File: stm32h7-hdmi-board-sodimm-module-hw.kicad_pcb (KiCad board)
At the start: 6 copper layers, 67.6 x 27.8 mm, 90 parts, among them J1 PCB-Edge_SODIMM_144_SDR, U1 IS42S86400F-7TL, U10 24AA024_TDFN, U2 IS42S86400F-7TL, U3 IS42S86400F-7TL, U4 IS42S86400F-7TL, U5 IS42S86400F-7TL, U6 IS42S86400F-7TL, U7 IS42S86400F-7TL, U8 IS42S86400F-7TL

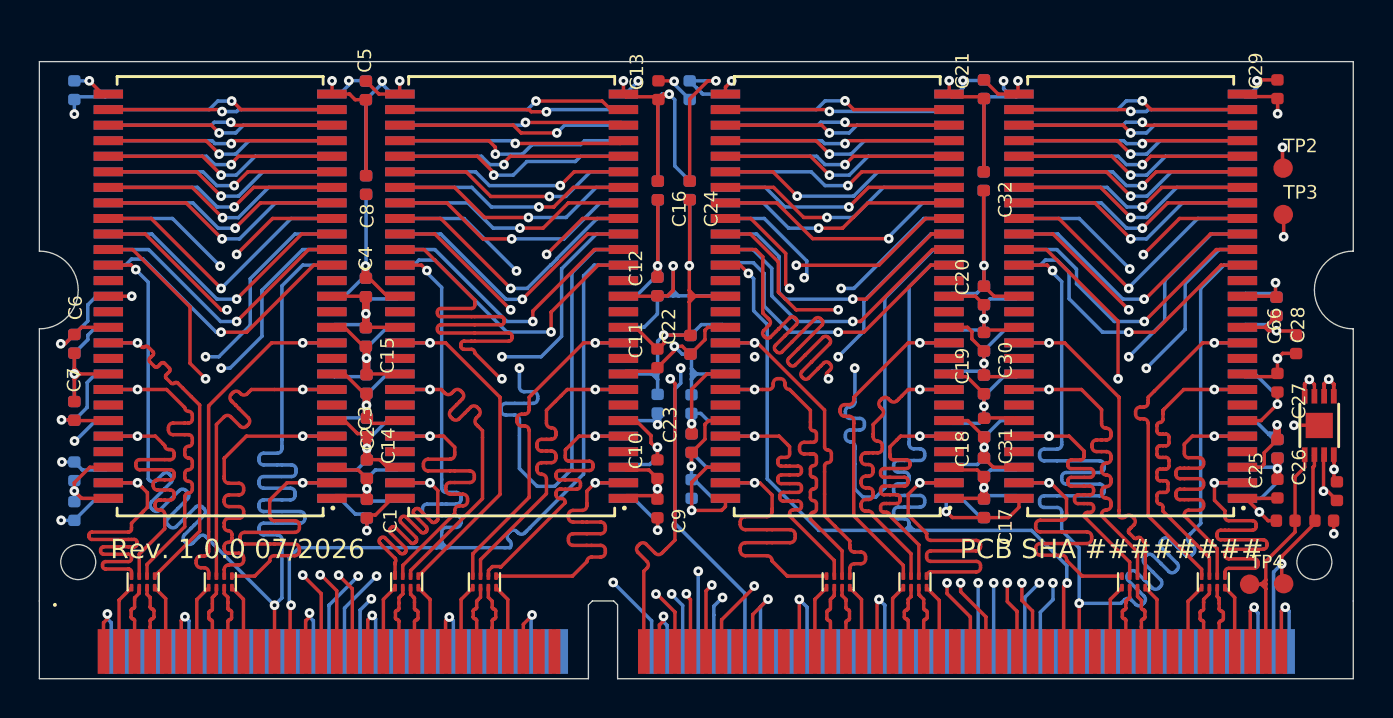
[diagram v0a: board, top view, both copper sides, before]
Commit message: [#101386] Matching ADDR bus
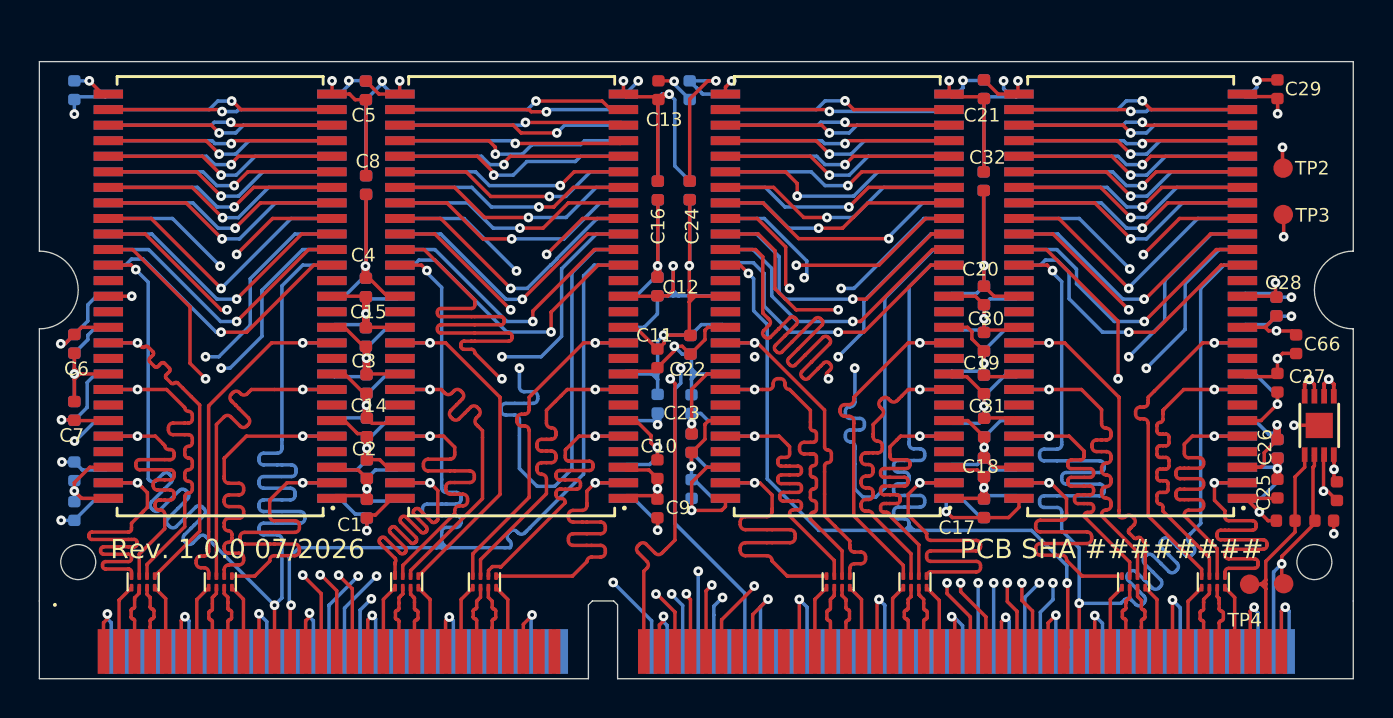
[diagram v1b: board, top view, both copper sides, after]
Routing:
- net GND: track 231.5 -> 247.7 mm, vias 42 -> 46
- net +3.3V: track 230.6 -> 244.7 mm, vias 37 -> 41
